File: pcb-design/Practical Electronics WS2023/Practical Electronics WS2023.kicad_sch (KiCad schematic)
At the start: 37 parts, among them J1 PWR Jack, J2 MIDI Input, J3 MIDI Thru out, J4 Conn_01x03, J5 ISP, U1 6N138, U1 ATmega328P-P, U2 LM2574Y-5 Buck converter, U3 74HCT04, Y1 Crystal

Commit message: Update voltage regulator
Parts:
- removed C1: 220uF, symbol Device:C_Polarized
- removed C2: 22uF, symbol Device:C_Polarized
- removed D10, D11, D12, D13, D14, D15, D16, D17, D3, D4, D5, D6, D7, D8, D9: WS2812B, LED_SMD:LED_WS2812B_PLCC4_5.0x5.0mm_P3.2mm, symbol LED:WS2812B
- removed D2: 11DQ05, symbol Device:D_Schottky
- removed U2: LM2574Y-5 Buck converter, Package_SO:SOIC-14W_7.5x9mm_P1.27mm, symbol Regulator_Switching:LM2574M-5
- added C1: 10uF 25V, symbol Device:C
- added C2: 0.1uF, symbol Device:C
- added C5: 47uF 6.3V, symbol Device:C
- added D18: PWR_LED_Green, symbol Device:LED
- added D2: SSB43L, symbol Device:D
- added R6: 100k, symbol Device:R
- added U2: ADP2303ARDZ-5.0, Package_SO:SOIC-8-1EP_3.9x4.9mm_P1.27mm_EP2.29x3mm, symbol Regulator_Switching:ADP2303ARDZ-5.0
- L1: value 330uH -> 4.7uH
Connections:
- net +12V: now also C1.1, R6.1, U2.2 (Vin), U2.3 (EN)
- net +5V: now also C5.1, D18.2 (A), U2.5 (FB)
- net GND: now also C1.2, C5.2, D18.1 (K), D2.2 (A), U2.7 (GND), U2.9 (PADGND)
- net LED_ON_BOARD: now also U1.2 (PD0)
- net at L1.1: now also C2.2, D2.1 (K), U2.8 (SW)
- new net: R6.2, U2.4 (PGOOD)
- new net: C2.1, U2.1 (BST)
- no-connect marks 29 -> 28
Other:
- moved on the sheet: D1, J1, J2, J4, J5, R2, R3, R4, U1

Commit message: Power switch, logic switches, LED strip detection, onboard LEDs are 2x8.
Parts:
- added Q1: Q_NMOS_DGS, symbol Device:Q_NMOS_DGS
- added R8: 10k, symbol Device:R
- added SW1, SW3: SW_DIP_x01, symbol Switch:SW_DIP_x01
- added SW2: SW_Push_SPDT, symbol Switch:SW_Push_SPDT
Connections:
- net +12V: now also SW2.1 (A); no longer J1.1
- net GND: now also Q1.1 (D), R8.2, SW1.2, SW3.2; no longer J4.1 (Pin_1)
- net at U1.12 (PD6): now also SW3.1
- net at U1.13 (PD7): now also SW1.1
- net at U1.3 (PD1): now also Q1.3 (S)
- net LED_ON_BOARD renamed ONBOARD LED DATA
- new net: J1.1, SW2.2 (B)
- new net LED GND: J4.1 (Pin_1), Q1.2 (G), R8.1
- no-connect marks 28 -> 26
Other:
- note added: "LED strip detector"
- note added: "Mode Switches"
- note added: "When LED is connected PIN3 is LOW. Internal pull-up resistor should be used."
- note added: "When switch is engaged - PIN is LOW. Internal pull-up resistors should be used."
- moved on the sheet: C1, C2, C5, D18, D2, J1, J3, J4, J5, L1, R1, R5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

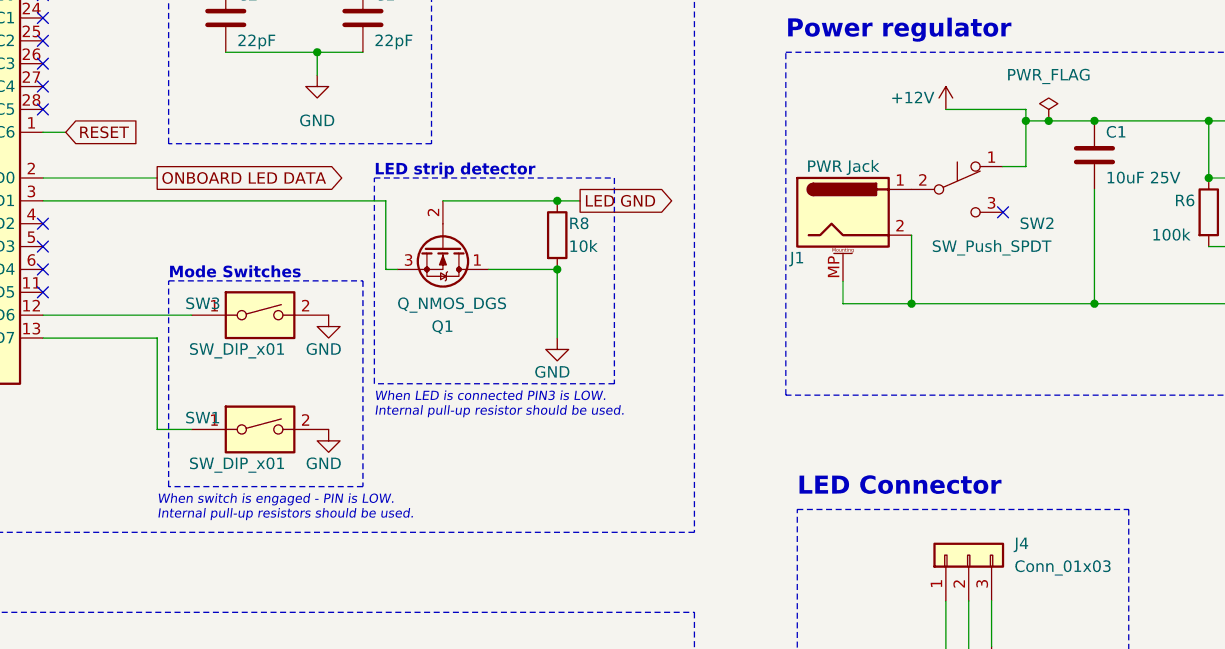
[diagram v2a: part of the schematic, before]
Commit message: Updated switches to match toggle switch pin configurations
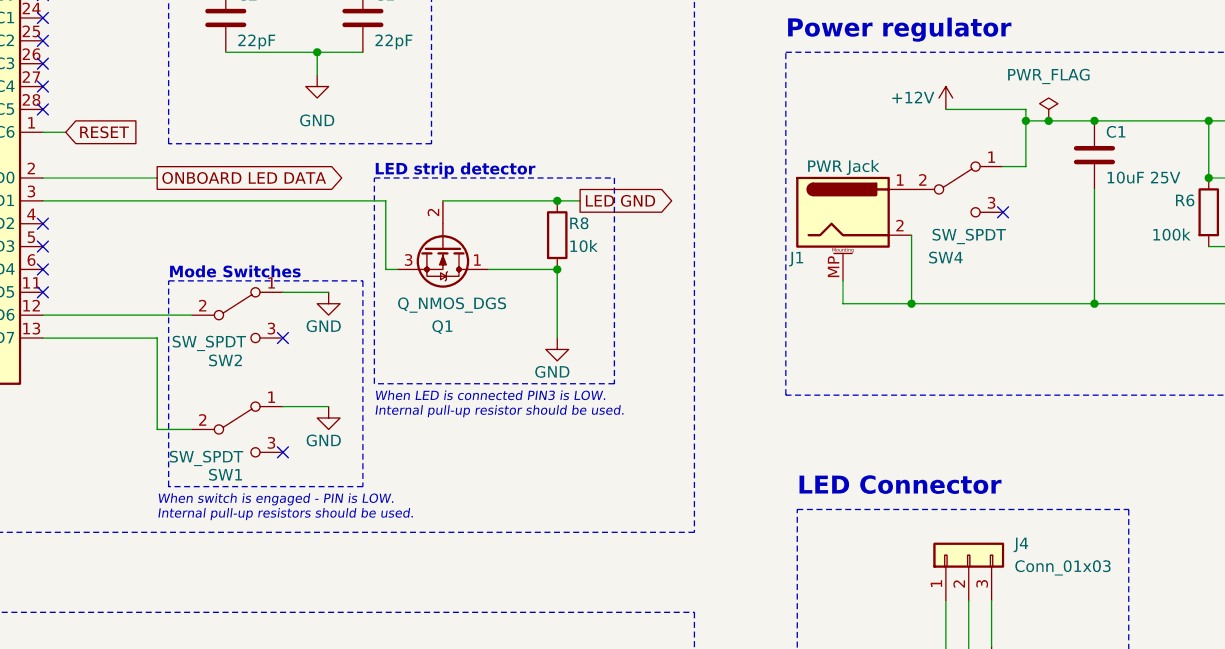
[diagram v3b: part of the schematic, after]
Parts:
- removed SW1, SW3: SW_DIP_x01, symbol Switch:SW_DIP_x01
- removed SW2: SW_Push_SPDT, symbol Switch:SW_Push_SPDT
- added SW1, SW2, SW4: SW_SPDT, symbol Switch:SW_SPDT
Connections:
- net +12V: now also SW4.1 (A)
- net GND: now also SW1.1 (A), SW2.1 (A)
- net at J1.1: now also SW4.2 (B)
- net at U1.12 (PD6): now also SW2.2 (B)
- net at U1.13 (PD7): now also SW1.2 (B)
- no-connect marks 26 -> 28

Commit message: Update schematic
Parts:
- removed R1, R5: 220, symbol Device:R_Small
- removed U3: 74HCT04, symbol 74xx:74HCT04
- added C1: 0.1uF, symbol Device:C
- added IC1: SN74LVC2G04DBVT, SOT95P280X145-6N, symbol SN74LVC2G04DBVT:SN74LVC2G04DBVT
- added R5, R7: 220, symbol Device:R
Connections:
- net +5V: now also C1.2, IC1.5 (VCC), R5.1
- net GND: now also J4.1 (Pin_1), C1.1, IC1.2 (GND)
- net LED GND: no longer J4.1 (Pin_1)
- net MIDI IN: now also IC1.1 (1A)
- net at J3.5: now also R7.2
- net at J3.4: now also R5.2
- new net: IC1.3 (2A), IC1.6 (1Y)
- new net: IC1.4 (2Y), R7.1
- no-connect marks 28 -> 20
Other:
- moved on the sheet: C1, C2, C5, D1, D18, D2, J1, J2, J3, J4, L1, R2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
